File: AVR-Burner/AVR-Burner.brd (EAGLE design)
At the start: 26 parts

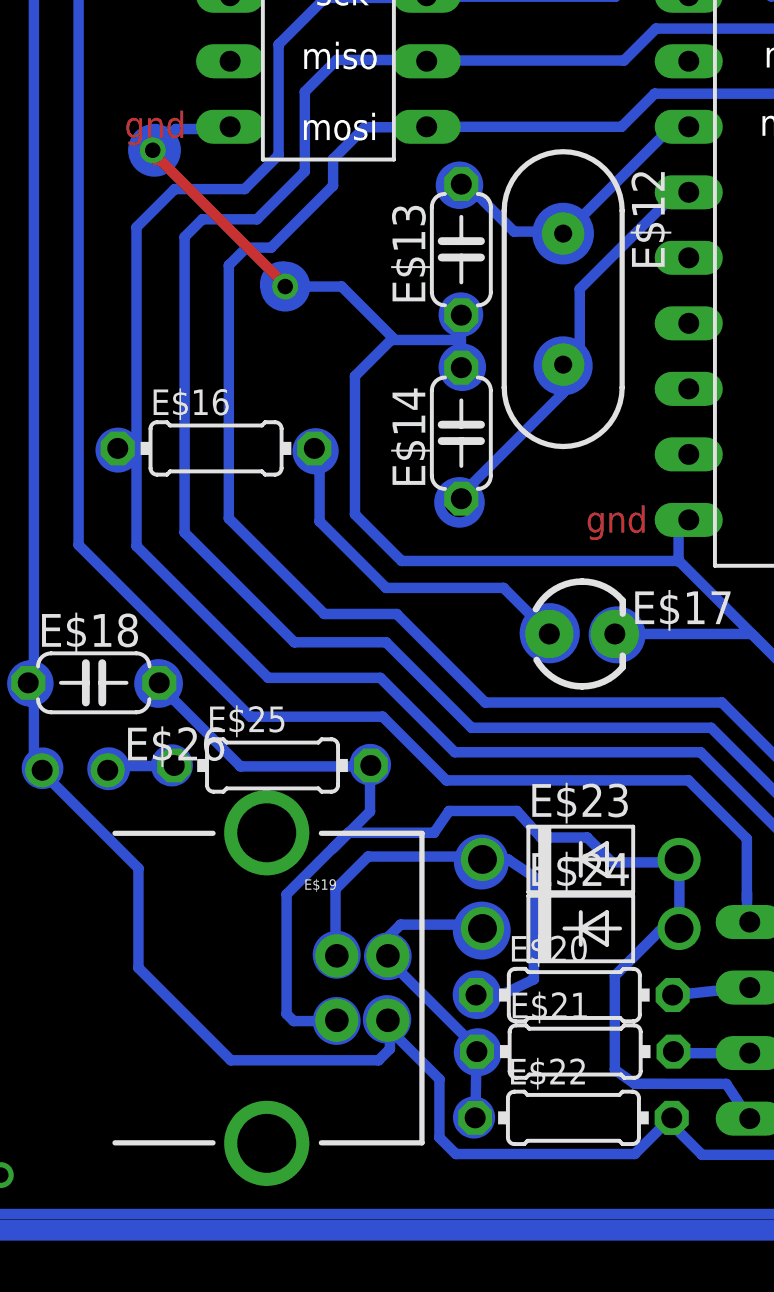
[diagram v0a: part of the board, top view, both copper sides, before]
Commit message: Fixed GND connections on AVR-Burner (Thanks Freddie)
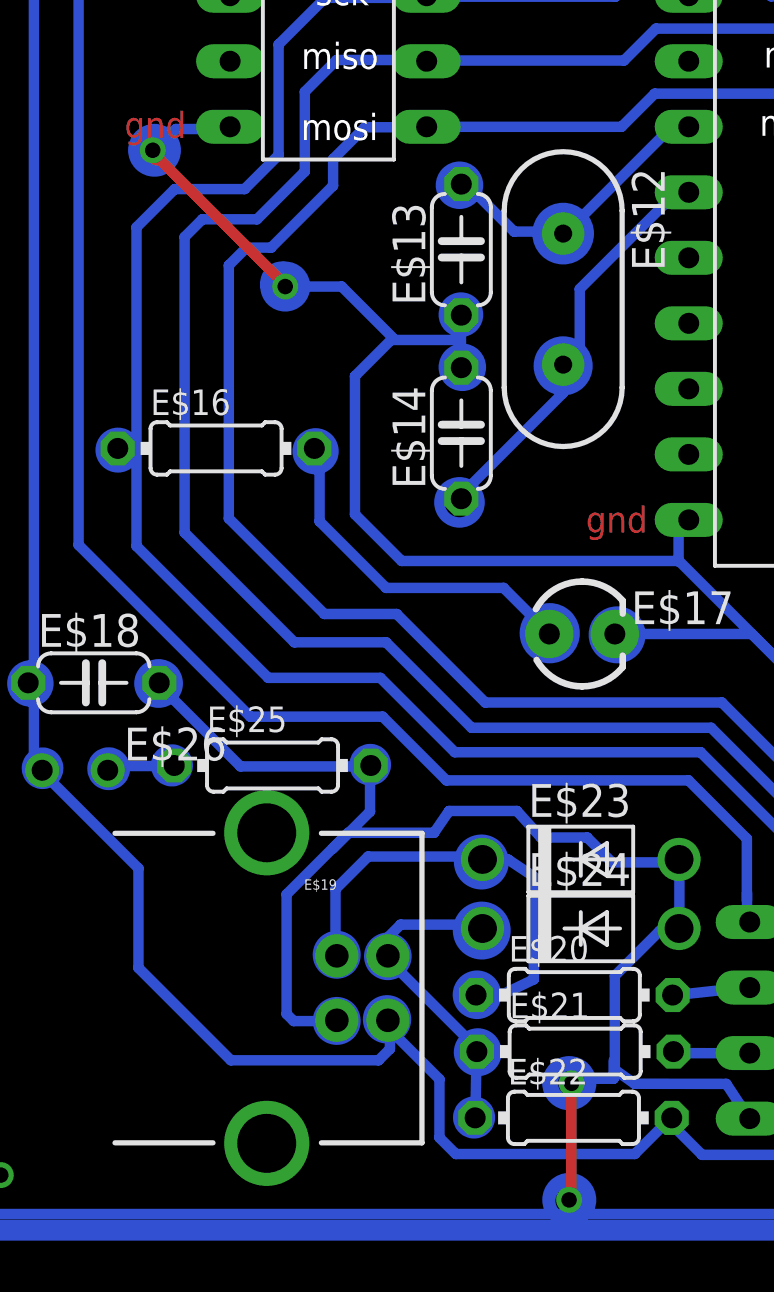
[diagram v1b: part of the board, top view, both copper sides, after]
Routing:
- net S$103: track 7.19 -> 14.2 mm
- net S$110: track 0.00 -> 4.73 mm
- net S$109: track 0.00 -> 1.80 mm
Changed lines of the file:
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@@
 <circle x="1.146859375" y="19.058421875" radius="0.697625" width="0.4064" layer="16"/>
 <circle x="6.11658125" y="19.058421875" radius="0.742296875" width="0.4064" layer="16"/>
+<circle x="21.9986125" y="-1.000846875" radius="0.69855625" width="0.4064" layer="16"/>
+<circle x="22.07860625" y="3.563015625" radius="0.68009375" width="0.4064" layer="16"/>
+<circle x="22.038609375" y="3.563015625" radius="0.847615625" width="0.4064" layer="16"/>
+<circle x="22.038609375" y="-0.9608125" radius="0.843753125" width="0.4064" layer="16"/>
 </plain>
 <attributes>
@@
 <wire x1="5.995653125" y1="39.35161875" x2="6.180103125" y2="39.35161875" width="0.4064" layer="1"/>
 <wire x1="6.180103125" y1="39.35161875" x2="11.134784375" y2="34.3969375" width="0.4064" layer="1"/>
+<wire x1="6.180103125" y1="39.35161875" x2="11.134784375" y2="34.3969375" width="0.4064" layer="1"/>
 </signal>
 <signal name="S$104">
@@
 <wire x1="9.29294375" y1="15.843746875" x2="6.154809375" y2="18.98188125" width="0.4064" layer="16"/>
 </signal>
+<signal name="S$107">
+<via x="22.12711875" y="3.556434375" extent="1-16" drill="0.6" shape="square"/>
+</signal>
+<signal name="S$108">
+<via x="22.031121875" y="-0.961196875" extent="1-16" drill="0.6" shape="square"/>
+</signal>
+<signal name="S$109">
+<wire x1="22.65886875" y1="3.735246875" x2="23.758490625" y2="3.735246875" width="0.4064" layer="16"/>
+<wire x1="23.758490625" y1="3.735246875" x2="23.758490625" y2="4.43560625" width="0.4064" layer="16"/>
+</signal>
+<signal name="S$110">
+<wire x1="22.005778125" y1="-1.03765" x2="22.120990625" y2="-1.03765" width="0.4064" layer="1"/>
+<wire x1="22.120990625" y1="-1.03765" x2="22.120990625" y2="3.57413125" width="0.4064" layer="1"/>
+</signal>
 </signals>
